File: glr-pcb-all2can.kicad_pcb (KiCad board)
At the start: 4 copper layers, 64 x 40 mm, 15 parts, among them IC1 TLE6250GV33XUMA1, IC2 TLE6250GV33XUMA1

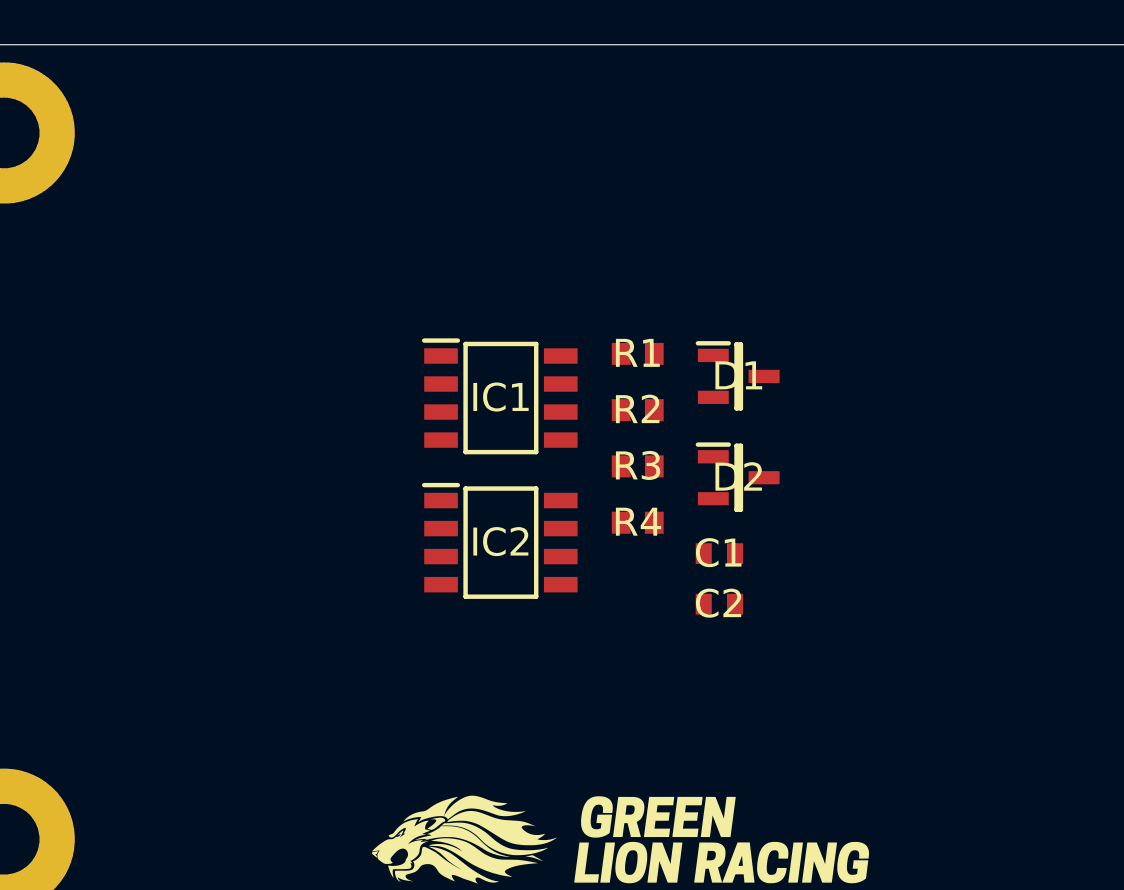
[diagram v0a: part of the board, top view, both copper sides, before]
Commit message: add main chip stm32f303k8t6
add two status leds
add debug/flash pins
connect first pins
remove second canbus
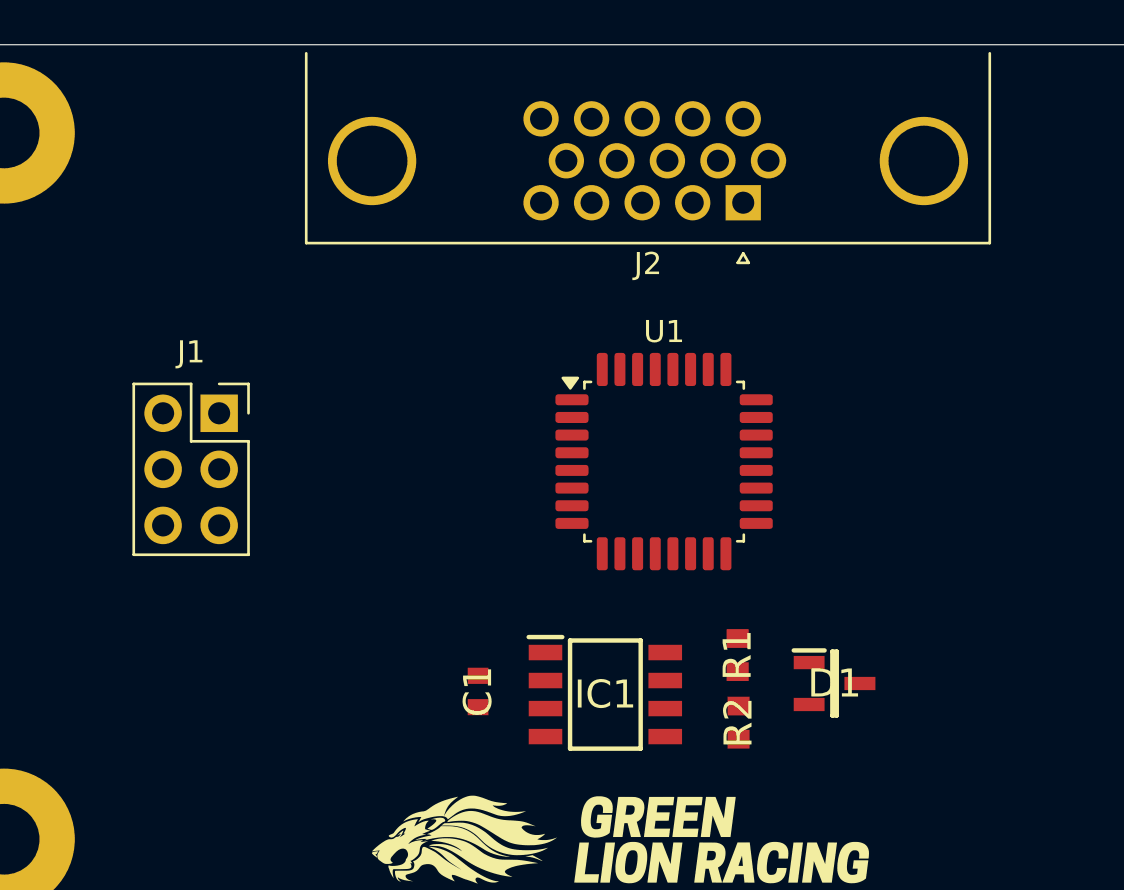
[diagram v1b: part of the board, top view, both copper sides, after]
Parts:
- removed C2: 0.1μF 50V, SamacSys_Parts:CAPC1608X90N
- removed D2: ESDCAN01-2BLY, SamacSys_Parts:SOT95P255X125-3N
- removed IC2: TLE6250GV33XUMA1, SamacSys_Parts:SOIC127P600X175-8N
- removed R3, R4: 120.0 Ω, SamacSys_Parts:RESC1608X50N
- added J1: Conn_02x04_Top_Bottom, Connector_PinSocket_2.54mm:PinSocket_2x03_P2.54mm_Vertical, F.Cu at (131.7, 106.7)
- added J2: DA15_Pins_MountingHoles, Connector_Dsub:DSUB-15-HD_Pins_Horizontal_P2.29x1.90mm_EdgePinOffset3.03mm_Housed_MountingHolesOffset4.94mm, F.Cu at (155.5, 97.2)
- added U1: STM32F303K8T6, Package_QFP:LQFP-32_7x7mm_P0.8mm, F.Cu at (151.9, 108.9)
- moved R2 14.9 mm to (155.3, 120.7), turned to 90 degrees
- moved D1 14.6 mm to (159.6, 118.9)
- moved R1 14.4 mm to (155.2, 117.7), turned to 90 degrees
- moved IC1 14.2 mm to (149.2, 119.4)
- moved C1 12.6 mm to (143.5, 119.3), turned to 90 degrees
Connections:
- D1 pad 1: /CAN Transciever/CAN H 2 -> /CAN Transciever/CAN H 1
- D1 pad 2: /CAN Transciever/CAN L 2 -> /CAN Transciever/CAN L 1
- IC1 pad 1: /CAN Transciever/TX 2 -> /CAN Transciever/TX 1
- IC1 pad 4: /CAN Transciever/RX 2 -> /CAN Transciever/RX 1
- IC1 pad 6: /CAN Transciever/CAN L 2 -> /CAN Transciever/CAN L 1
- IC1 pad 7: /CAN Transciever/CAN H 2 -> /CAN Transciever/CAN H 1
- R1 pad 2: /CAN Transciever/CAN H 2 -> /CAN Transciever/CAN H 1
- R2 pad 1: /CAN Transciever/CAN L 2 -> /CAN Transciever/CAN L 1

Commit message: add in- and outputs
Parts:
- added C7: 0.1μF 50V, SamacSys_Parts:CAPC1608X90N, F.Cu at (128.8, 121.4)
- added D10: BAT54S, Package_TO_SOT_SMD:SOT-23, F.Cu at (171.3, 103.2)
- added D11: BAT54S, Package_TO_SOT_SMD:SOT-23, F.Cu at (171.3, 107.8)
- added D12: BAT54S, Package_TO_SOT_SMD:SOT-23, F.Cu at (171.3, 112.5)
- added D5: ESDCAN01-2BLY, SamacSys_Parts:SOT95P255X125-3N, F.Cu at (129.6, 118.0)
- added D6: BAT54S, Package_TO_SOT_SMD:SOT-23, F.Cu at (166.3, 103.2)
- added D7: BAT54S, Package_TO_SOT_SMD:SOT-23, F.Cu at (166.3, 107.8)
- added D8: BAT54S, Package_TO_SOT_SMD:SOT-23, F.Cu at (166.3, 112.5)
- added D9: BAT54S, Package_TO_SOT_SMD:SOT-23, F.Cu at (166.3, 117.1)
- added J3: Conn_01x04, Connector_PinSocket_2.54mm:PinSocket_1x04_P2.54mm_Vertical, F.Cu at (141.2, 103.1)
- added Q1: DMN6075S, Package_TO_SOT_SMD:SOT-23, F.Cu at (178.2, 103.2)
- added Q2: DMN6075S, Package_TO_SOT_SMD:SOT-23, F.Cu at (178.2, 107.8)
- added Q3: DMN6075S, Package_TO_SOT_SMD:SOT-23, F.Cu at (178.2, 112.5)
- added Q4: DMN6075S, Package_TO_SOT_SMD:SOT-23, F.Cu at (178.2, 117.1)
- added R5: 120.0 Ω, SamacSys_Parts:RESC1608X50N, F.Cu at (125.1, 116.9)
- added R6: 120.0 Ω, SamacSys_Parts:RESC1608X50N, F.Cu at (125.1, 119.5)
- added U2: 173020536, MagIC_THT_Wurth:U_Wurth_MagIC-FDSM_17302xx36, F.Cu at (127.3, 102.8)
- added U3: 173010535, MagIC_THT_Wurth:U_Wurth_MagIC-FDSM_17301xx35, F.Cu at (114.3, 106.8)
- C1: value 0.1μF 50V -> 1uF
- D1: value ESDCAN01-2BLY -> LED
- J1: value Conn_02x04_Top_Bottom -> DA15_Pins_MountingHoles; footprint Connector_PinSocket_2.54mm:PinSocket_2x03_P2.54mm_Vertical -> Connector_Dsub:DSUB-15-HD_Pins_Horizontal_P2.29x1.90mm_EdgePinOffset3.03mm_Housed_MountingHolesOffset4.94mm
- J2: value DA15_Pins_MountingHoles -> Conn_02x04_Top_Bottom; footprint Connector_Dsub:DSUB-15-HD_Pins_Horizontal_P2.29x1.90mm_EdgePinOffset3.03mm_Housed_MountingHolesOffset4.94mm -> Connector_PinSocket_2.54mm:PinSocket_2x03_P2.54mm_Vertical
- R1: value 120.0 Ω -> 100kR
- R2: value 120.0 Ω -> 120R
- moved J2 31.8 mm to (134.8, 121.3)
- moved J1 17.8 mm to (146.9, 97.3), turned to 180 degrees
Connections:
- net /CAN Transciever/RX 1 renamed /CAN transciever/RX 1
- net /CAN Transciever/TX 1 renamed /CAN transciever/TX 1
- C1 pad 1: +5V -> GND
- C1 pad 2: GND -> +3V3
- D1 pad 1: /CAN Transciever/CAN H 1 -> Net-(D1-K)
- D1 pad 2: /CAN Transciever/CAN L 1 -> Net-(D1-A)
- D1 pad 3: GND -> (no net)
- IC1 pad 6: /CAN Transciever/CAN L 1 -> /CAN transciever/CAN L 1
- IC1 pad 7: /CAN Transciever/CAN H 1 -> /CAN transciever/CAN H 1
- J1 pad 1: Net-(J1-Pin_1) -> GND
- J1 pad 2: Net-(J1-Pin_2) -> +24V
- J1 pad 3: NRST -> /CAN transciever/CAN L 1
- J1 pad 4: GND -> /CAN transciever/CAN H 1
- J1 pad 5: +3.3V -> /Input filter/1_IN
- J1 pad 6: unconnected-(J1-Pin_6-Pad6) -> /Input filter/2_IN
- J2 pad 1: unconnected-(J2-Pad1) -> Net-(J2-Pin_1)
- J2 pad 2: unconnected-(J2-Pad2) -> Net-(J2-Pin_2)
- J2 pad 3: unconnected-(J2-Pad3) -> NRST
- J2 pad 4: unconnected-(J2-Pad4) -> GND
- J2 pad 5: unconnected-(J2-Pad5) -> +3V3
- R1 pad 1: Net-(R1-Pad1) -> +3V3
- R1 pad 2: /CAN Transciever/CAN H 1 -> NRST
- R2 pad 1: /CAN Transciever/CAN L 1 -> Net-(U1-BOOT0)
- R2 pad 2: Net-(R1-Pad1) -> GND
- U1 pad 1: +3.3V -> +3V3
- U1 pad 10: unconnected-(U1-PA4-Pad10) -> /Input filter/5_IN_INT
- U1 pad 11: unconnected-(U1-PA5-Pad11) -> /Input filter/6_IN_INT
- U1 pad 12: unconnected-(U1-PA6-Pad12) -> /Input filter/7_IN_INT
- U1 pad 14: unconnected-(U1-PB0-Pad14) -> /Output/1_OUT_INT
- U1 pad 15: unconnected-(U1-PB1-Pad15) -> /Output/2_OUT_INT
- U1 pad 17: +3.3V -> +3V3
- U1 pad 2: Net-(D2-K) (its old number) -> Net-(D1-K)
- U1 pad 23: Net-(J1-Pin_1) -> Net-(J2-Pin_1)
- U1 pad 24: Net-(J1-Pin_2) -> Net-(J2-Pin_2)
- U1 pad 25: unconnected-(U1-PA15-Pad25) -> Net-(J3-Pin_4)
- U1 pad 26: unconnected-(U1-PB3-Pad26) -> Net-(J3-Pin_1)
- U1 pad 27: unconnected-(U1-PB4-Pad27) -> Net-(J3-Pin_2)
- U1 pad 28: unconnected-(U1-PB5-Pad28) -> Net-(J3-Pin_3)
- U1 pad 29: unconnected-(U1-PB6-Pad29) -> /Output/3_OUT_INT
- U1 pad 30: unconnected-(U1-PB7-Pad30) -> /Output/4_OUT_INT
- U1 pad 5: +3.3V -> +3V3
- U1 pad 6: unconnected-(U1-PA0-Pad6) -> /Input filter/1_IN_INT
- U1 pad 7: unconnected-(U1-PA1-Pad7) -> /Input filter/2_IN_INT
- U1 pad 8: unconnected-(U1-PA2-Pad8) -> /3_IN_INT
- U1 pad 9: unconnected-(U1-PA3-Pad9) -> /Input filter/4_IN_INT

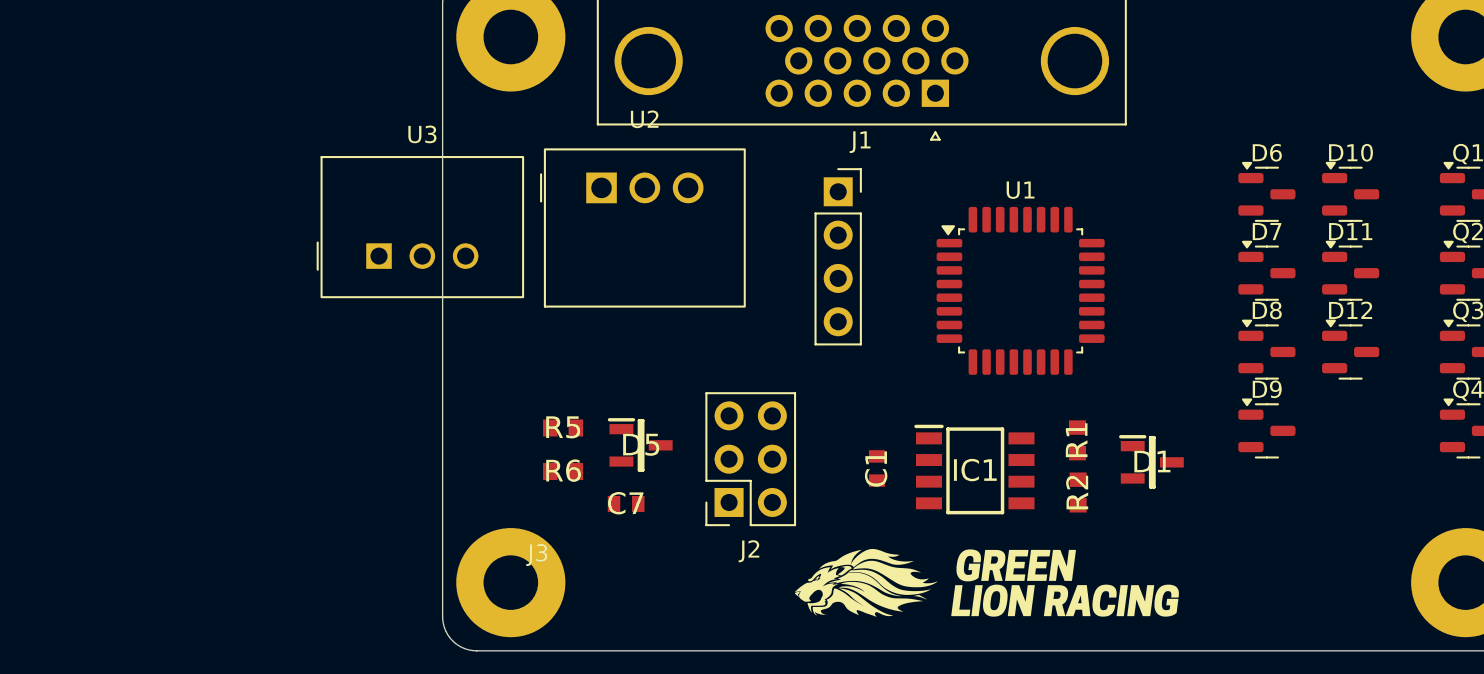
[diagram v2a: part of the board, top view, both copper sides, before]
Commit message: change voltage regulators
change can transciever
add more useful parts to can setup
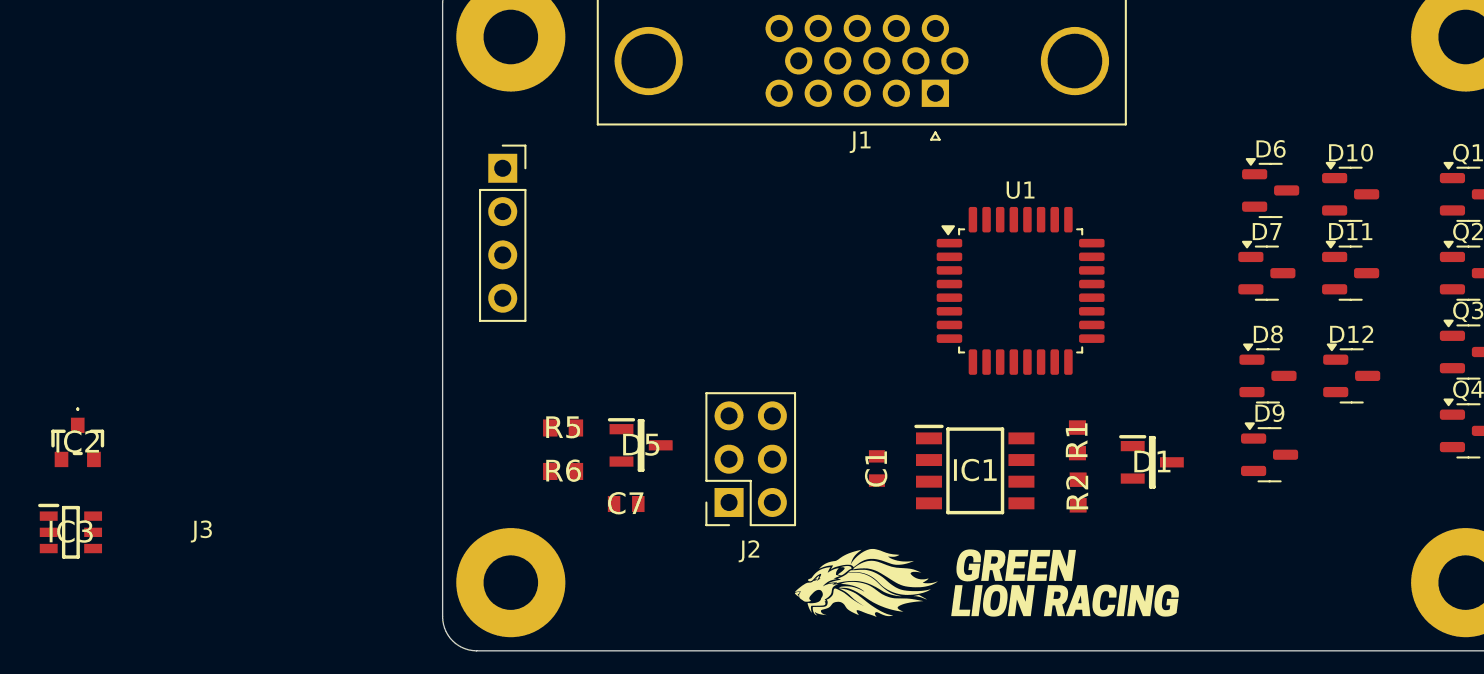
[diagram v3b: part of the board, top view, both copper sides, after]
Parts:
- removed U2: 173020536, MagIC_THT_Wurth:U_Wurth_MagIC-FDSM_17302xx36
- removed U3: 173010535, MagIC_THT_Wurth:U_Wurth_MagIC-FDSM_17301xx35
- added IC2: ZMR330FTA, SamacSys_Parts:ZMR330FTA, F.Cu at (96.6, 117.8)
- added IC3: AP64060WU-7, SamacSys_Parts:SOT95P280X100-6N, F.Cu at (96.2, 123.0)
- R1: value 100kR -> 100k
- moved J3 19.7 mm to (121.5, 101.7)
- moved D9 1.41 mm to (166.5, 118.5)
- moved D12 1.40 mm to (171.3, 113.9)
- moved D8 1.40 mm to (166.4, 113.9)
- moved D6 0.31 mm to (166.6, 103.0)
